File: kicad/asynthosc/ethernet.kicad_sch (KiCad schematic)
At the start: 40 parts, among them J12 RJ45_LED_Shielded, U10 LAN8742A, U11 USBLC6-2P6, U13 USBLC6-2P6, Y3 25MHZ,20PF,30PPM

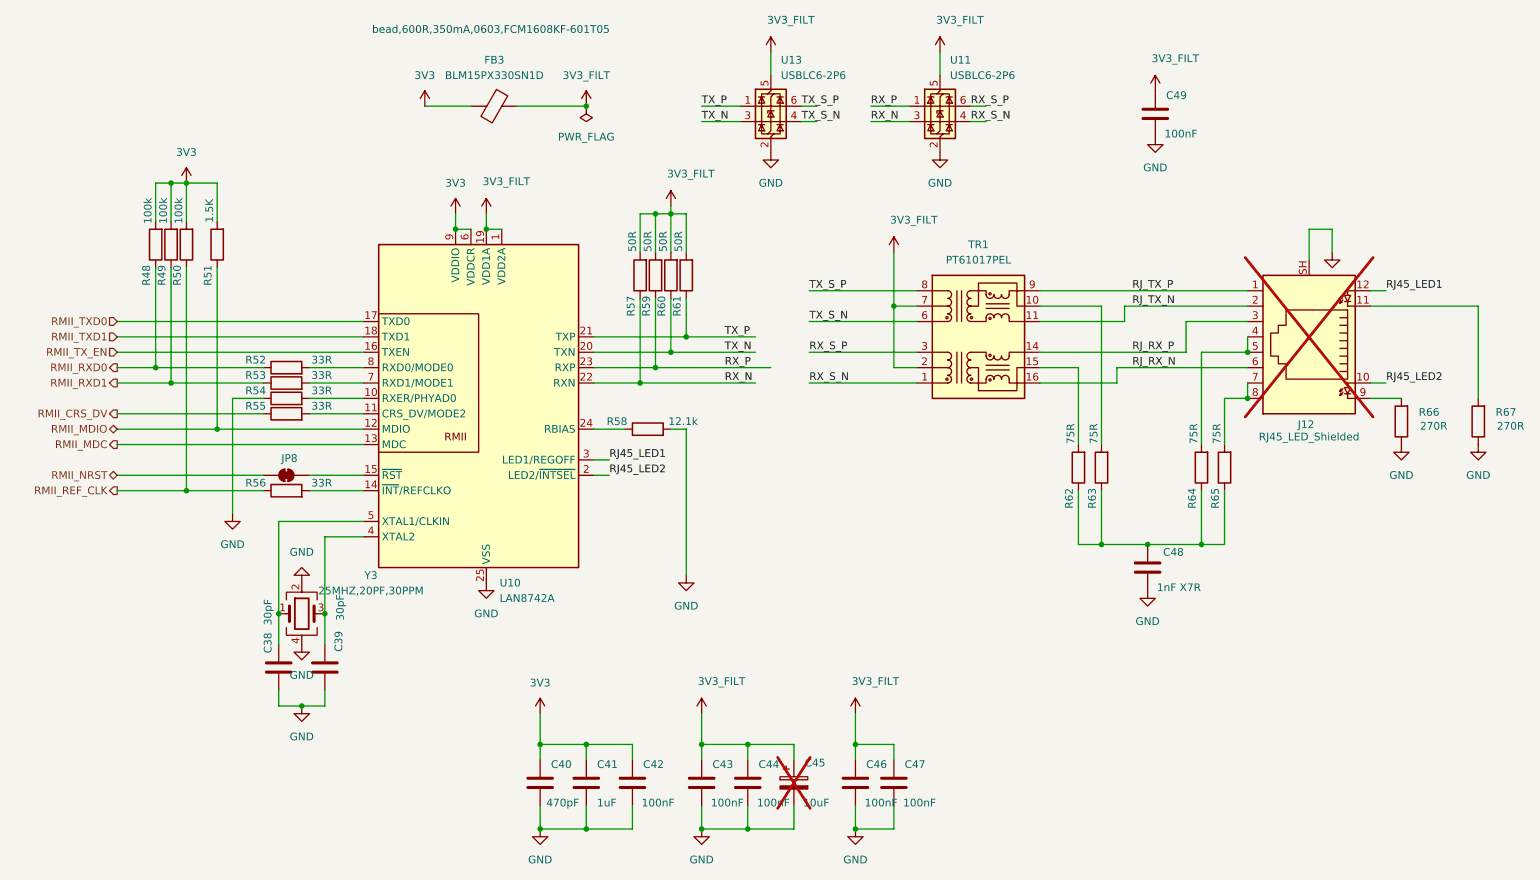
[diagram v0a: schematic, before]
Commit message: fix: ethernet stage pull-up resistors
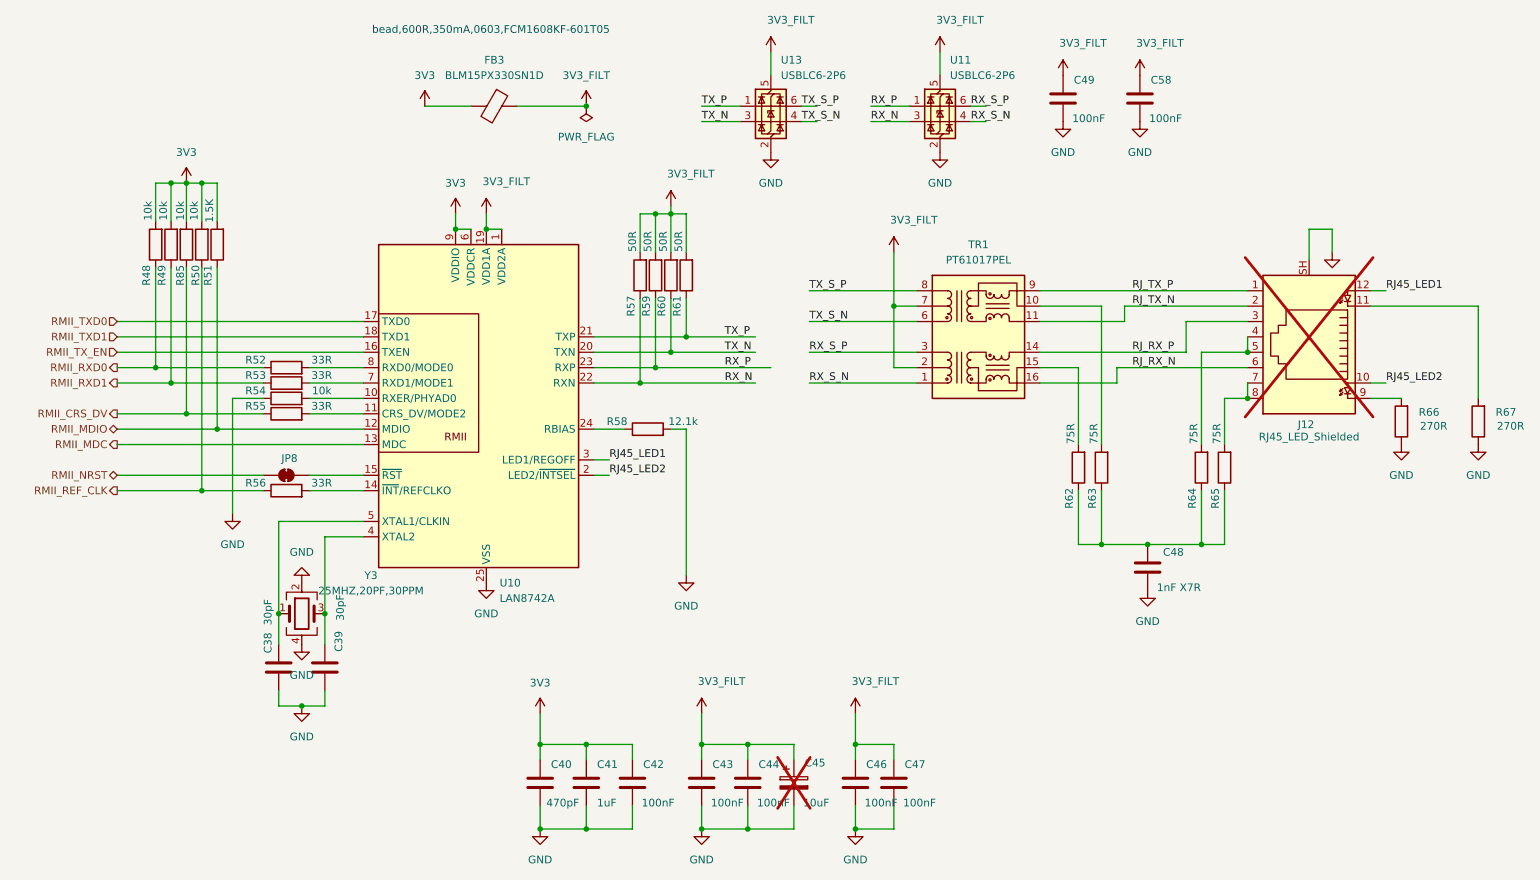
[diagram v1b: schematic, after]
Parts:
- added C58: 100nF, Capacitor_SMD:C_0402_1005Metric, symbol Device:C
- added R85: 10k, Resistor_SMD:R_0402_1005Metric, symbol Device:R
- R48, R49, R50: value 100k -> 10k
- R54: value 33R -> 10k
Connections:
- net 3V3: now also R85.2
- net 3V3_FILT: now also C58.1
- net GND: now also C58.2
- net RMII_CRS_DV: now also R85.1
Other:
- moved on the sheet: C49, R50

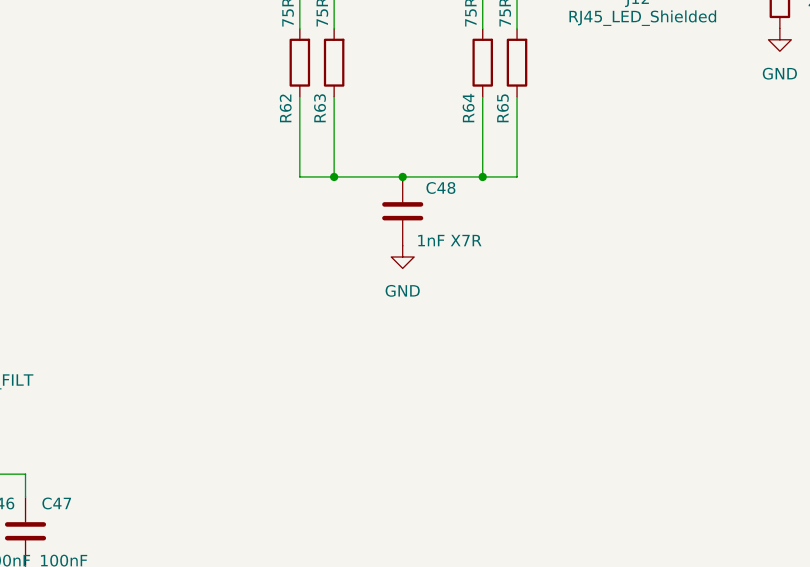
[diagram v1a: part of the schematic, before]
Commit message: fix: ethernet filtering capacitor size
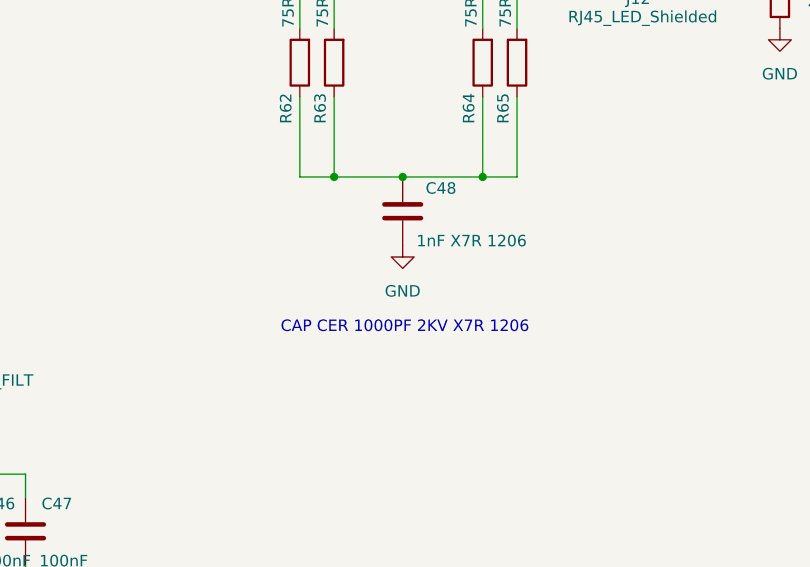
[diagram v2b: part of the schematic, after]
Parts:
- C48: value 1nF X7R -> 1nF X7R 1206; footprint Capacitor_SMD:C_0402_1005Metric -> Capacitor_SMD:C_1206_3216Metric
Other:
- note added: "CAP CER 1000PF 2KV X7R 1206"
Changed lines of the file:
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@@
+		)
+	)
+	(text "	\nCAP CER 1000PF 2KV X7R 1206"
+		(exclude_from_sim no)
+		(at 199.644 119.888 0)
+		(effects
+			(font
+				(size 1.27 1.27)
+			)
 		)
 	)
@@
 			)
 		)
-		(property "Value" "1nF X7R"
+		(property "Value" "1nF X7R 1206"
 			(at 200.914 111.252 0)
 			(effects
@@
 			)
 		)
-		(property "Footprint" "Capacitor_SMD:C_0402_1005Metric"
+		(property "Footprint" "Capacitor_SMD:C_1206_3216Metric"
 			(at 200.3552 111.76 0)
 			(effects

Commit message: bom: adding jlc ref to generic
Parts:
- C38, C39: LCSC (none) -> C1570
- C40: LCSC (none) -> C454372
- C41: LCSC (none) -> C28323
- C42, C43, C44, C46, C47, C49, C58: LCSC (none) -> C307331
- C48: LCSC (none) -> C382729
- R48, R49, R50, R54, R85: LCSC (none) -> C25744
- R51: LCSC (none) -> C102811
- R52, R53, R55, R56: LCSC (none) -> C25105
- R57, R59, R60, R61: LCSC (none) -> C227387
- R58: LCSC (none) -> C385272
- R62, R63, R64, R65: LCSC (none) -> C156124
- R66, R67: LCSC (none) -> C144055
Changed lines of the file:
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@@
 			)
 		)
-		(property "LCSC" ""
+		(property "LCSC" "C28323"
 			(at 106.68 143.51 0)
 			(effects
@@
 			)
 		)
-		(property "LCSC" ""
+		(property "LCSC" "C25744"
 			(at 35.56 54.61 0)
 			(effects
@@
 			)
 		)
-		(property "LCSC" ""
+		(property "LCSC" "C25105"
 			(at 57.15 82.55 0)
 			(effects
@@
 			)
 		)
-		(property "LCSC" ""
+		(property "LCSC" "C25744"
 			(at 57.15 80.01 0)
 			(effects
@@
 			)
 		)
-		(property "LCSC" ""
+		(property "LCSC" "C454372"
 			(at 99.06 143.51 0)
 			(effects
@@
 			)
 		)
-		(property "LCSC" ""
+		(property "LCSC" "C25105"
 			(at 57.15 74.93 0)
 			(effects
@@
 			)
 		)
-		(property "LCSC" ""
+		(property "LCSC" "C25105"
 			(at 57.15 77.47 0)
 			(effects
@@
 			)
 		)
-		(property "LCSC" ""
+		(property "LCSC" "C156124"
 			(at 187.96 91.44 0)
 			(effects
@@
 			)
 		)
-		(property "LCSC" ""
+		(property "LCSC" "C1570"
 			(at 55.88 124.46 0)
 			(effects
@@
 			)
 		)
-		(property "LCSC" ""
+		(property "LCSC" "C227387"
 			(at 115.57 59.69 0)
 			(effects
@@
 			)
 		)
-		(property "LCSC" ""
+		(property "LCSC" "C1570"
 			(at 63.5 124.46 0)
 			(effects
@@
 			)
 		)
-		(property "LCSC" ""
+		(property "LCSC" "C144055"
 			(at 241.3 83.82 0)
 			(effects
@@
 			)
 		)
-		(property "LCSC" ""
+		(property "LCSC" "C307331"
 			(at 125.73 143.51 0)
 			(effects
@@
 			)
 		)
-		(property "LCSC" ""
+		(property "LCSC" "C382729"
 			(at 199.39 107.95 0)
 			(effects
@@
 			)
 		)
-		(property "LCSC" ""
+		(property "LCSC" "C227387"
 			(at 120.65 59.69 0)
 			(effects
@@
 			)
 		)
-		(property "LCSC" ""
+		(property "LCSC" "C385272"
 			(at 116.84 85.09 0)
 			(effects
@@
 			)
 		)
-		(property "LCSC" ""
+		(property "LCSC" "C227387"
 			(at 118.11 59.69 0)
 			(effects
@@
 			)
 		)
-		(property "LCSC" ""
+		(property "LCSC" "C307331"
 			(at 151.13 143.51 0)
 			(effects
@@
 			)
 		)
-		(property "LCSC" ""
+		(property "LCSC" "C307331"
 			(at 114.3 143.51 0)
 			(effects
@@
 			)
 		)
-		(property "LCSC" ""
+		(property "LCSC" "C227387"
 			(at 123.19 59.69 0)
 			(effects
@@
 			)
 		)
-		(property "LCSC" ""
+		(property "LCSC" "C144055"
 			(at 254 83.82 0)
 			(effects
@@
 			)
 		)
-		(property "LCSC" ""
+		(property "LCSC" "C156124"
 			(at 191.77 91.44 0)
 			(effects
@@
 			)
 		)
-		(property "LCSC" ""
+		(property "LCSC" "C25744"
 			(at 43.18 54.61 0)
 			(effects
@@
 			)
 		)
-		(property "LCSC" ""
+		(property "LCSC" "C25744"
 			(at 38.1 54.61 0)
 			(effects
@@
 			)
 		)
-		(property "LCSC" ""
+		(property "LCSC" "C156124"
 			(at 208.28 91.44 0)
 			(effects
@@
 			)
 		)
-		(property "LCSC" ""
+		(property "LCSC" "C307331"
 			(at 133.35 143.51 0)
 			(effects
@@
 			)
 		)
-		(property "LCSC" ""
+		(property "LCSC" "C307331"
 			(at 157.48 143.51 0)
 			(effects
@@
 			)
 		)
-		(property "LCSC" ""
+		(property "LCSC" "C25105"
 			(at 57.15 95.25 0)
 			(effects
@@
 			)
 		)
-		(property "LCSC" ""
+		(property "LCSC" "C156124"
 			(at 212.09 91.44 0)
 			(effects
@@
 			)
 		)
-		(property "LCSC" ""
+		(property "LCSC" "C102811"
 			(at 45.72 54.61 0)
 			(effects
@@
 			)
 		)
-		(property "LCSC" ""
+		(property "LCSC" "C307331"
 			(at 198.12 30.48 0)
 			(effects
@@
 			)
 		)
-		(property "LCSC" ""
+		(property "LCSC" "C25744"
 			(at 40.64 54.61 0)
 			(effects
@@
 			)
 		)
-		(property "LCSC" ""
+		(property "LCSC" "C307331"
 			(at 185.42 30.48 0)
 			(effects

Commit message: bom: update jlcpcb part numbers
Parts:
- C40: LCSC C454372 -> C295986
- C48: JLC 0402 -> 1206; LCSC C382729 -> C9196
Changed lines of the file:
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@@
 			)
 		)
-		(property "LCSC" "C454372"
+		(property "LCSC" " C295986"
 			(at 99.06 143.51 0)
 			(effects
@@
 			)
 		)
-		(property "LCSC" "C382729"
+		(property "LCSC" " C9196"
 			(at 199.39 107.95 0)
 			(effects
@@
 			)
 		)
-		(property "JLC" "0402"
+		(property "JLC" "1206"
 			(at 199.39 107.95 0)
 			(effects

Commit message: sch: update bom
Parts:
- R58: LCSC C385272 -> C321280
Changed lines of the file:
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@@
 			)
 		)
-		(property "LCSC" "C385272"
+		(property "LCSC" "C321280"
 			(at 116.84 85.09 0)
 			(effects
